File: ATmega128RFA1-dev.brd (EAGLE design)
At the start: 36.8 x 71.1 mm, 44 parts, among them J1 POWER_JACKSMD, J2 AVR_SPI_PRG_6PTH, Q1 16MHz, Q2 32.768kHz, U1 ATMEGA128RFA1, U2 V_REG_LDOSMD, Y1 ANTENNA2SMD5

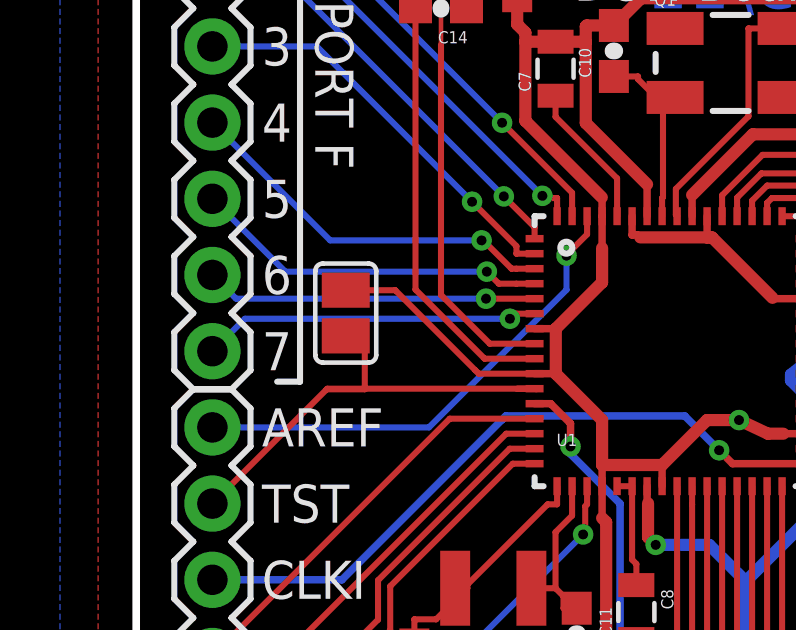
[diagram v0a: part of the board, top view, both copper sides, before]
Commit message: Added trace so solder jumper is connected until you cut it.
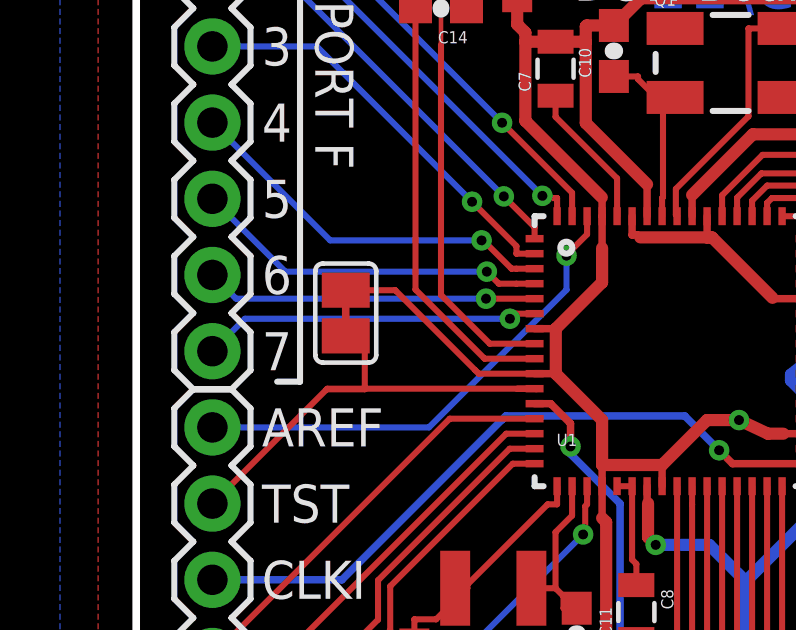
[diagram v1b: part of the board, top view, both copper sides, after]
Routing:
- net TST: track 17.4 -> 18.8 mm
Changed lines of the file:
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@@
 <wire x1="13.335" y1="45.74" x2="13.28" y2="45.74" width="0.2032" layer="1"/>
 <wire x1="13.28" y1="45.74" x2="12.7" y2="45.74" width="0.2032" layer="1"/>
+<wire x1="6.985" y1="47.498" x2="6.985" y2="48.895" width="0.254" layer="1"/>
 </signal>
 <signal name="AREF">
@@
 </signal>
 </signals>
-<errors>
-</errors>
 </board>
 </drawing>

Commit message: Rearranged CC message so more of the board fits on my display
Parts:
- removed U$1: CREATIVE_COMMONS, SparkFun:CREATIVE_COMMONS
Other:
- board text added: "Creative Commons Attribution"
- board text added: "Designed by:"
- board text added: "Released under the"
- board text added: "Share-Alike 3.0 License"
- board text added: "http://creativecommons.org/licenses/by-sa/3.0"
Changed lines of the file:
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@@
 <text x="28.448" y="2.921" size="1.27" layer="21" font="vector" ratio="15" rot="R90">RX1</text>
 <text x="30.988" y="2.921" size="1.27" layer="21" font="vector" ratio="15" rot="R90">TX1</text>
-<text x="49.53" y="-35.56" size="1.778" layer="27" font="vector" ratio="15">Ryan Owens</text>
 <text x="13.208" y="5.842" size="1.27" layer="21" ratio="16">AVR ISP</text>
+<text x="43.18" y="55.88" size="1.778" layer="23">Released under the</text>
+<text x="43.18" y="52.07" size="1.778" layer="23">Creative Commons Attribution</text>
+<text x="43.18" y="48.26" size="1.778" layer="23">Share-Alike 3.0 License</text>
+<text x="43.18" y="44.45" size="1.778" layer="23">http://creativecommons.org/licenses/by-sa/3.0</text>
+<text x="43.18" y="40.64" size="1.778" layer="23">Designed by:</text>
+<text x="43.18" y="36.83" size="1.778" layer="23" ratio="16">Ryan Owens</text>
 </plain>
 <attributes>
@@
 <attribute name="VALUE" x="21.971" y="-1.651" size="1.27" layer="27"/>
 </element>
-<element name="U$1" library="SparkFun" package="CREATIVE_COMMONS" value="CREATIVE_COMMONS" x="19.05" y="-35.56"/>
 <element name="SJ1" library="jumper" package="SJ" value="" x="6.985" y="48.26" smashed="yes" rot="R270">
 <attribute name="VALUE" x="6.985" y="47.8599" size="0.02" layer="27" rot="R270"/>
